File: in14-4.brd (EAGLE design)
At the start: 160 x 39 mm, 15 parts, among them IC1 4094D, IC2 4094D, Q1 K155ID1, Q2 K155ID1, Q3 K155ID1, Q4 K155ID1

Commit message: Existing files added
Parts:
- moved IC2 24.5 mm to (97.3, 30.2)
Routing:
- net N$34: track 0.00 -> 50.4 mm
- net N$33: track 0.00 -> 44.9 mm
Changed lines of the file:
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@@
 <setting verticaltext="up"/>
 </settings>
-<grid distance="0.00625" unitdist="inch" unit="inch" style="dots" multiple="1" display="yes" altdistance="0.025" altunitdist="inch" altunit="inch"/>
+<grid distance="0.0125" unitdist="inch" unit="inch" style="dots" multiple="1" display="yes" altdistance="0.025" altunitdist="inch" altunit="inch"/>
 <layers>
 <layer number="1" name="Top" color="4" fill="1" visible="yes" active="yes"/>
@@
 <element name="Q4" library="nixie" package="DIL16" value="K155ID1" x="110.49" y="54.61" rot="MR180"/>
 <element name="UL4" library="nixie" package="IN-14" value="IN-14" x="110.49" y="40.64" rot="R180"/>
-<element name="IC2" library="40xx" package="SO16" value="4094D" x="72.86625" y="30.7975" rot="MR180"/>
+<element name="IC2" library="40xx" package="SO16" value="4094D" x="97.31375" y="30.1625" rot="MR180"/>
 <element name="R3" library="rcl" package="R1206" value="10K" x="82.55" y="33.02" rot="MR0"/>
 <element name="R4" library="rcl" package="R1206" value="10K" x="106.68" y="33.02" rot="MR0"/>
@@
 <wire x1="46.99" y1="59.69" x2="46.99" y2="58.42" width="0.4064" layer="1"/>
 <wire x1="87.63" y1="58.42" x2="111.76" y2="58.42" width="0" layer="19" extent="1-1"/>
-<wire x1="77.31125" y1="33.8709" x2="87.63" y2="58.42" width="0" layer="19" extent="16-16"/>
-<wire x1="68.42125" y1="27.7241" x2="77.31125" y2="33.8709" width="0" layer="19" extent="16-16"/>
-<wire x1="36.03625" y1="32.6009" x2="68.42125" y2="27.7241" width="0" layer="19" extent="16-16"/>
+<wire x1="101.75875" y1="33.2359" x2="87.63" y2="58.42" width="0" layer="19" extent="16-16"/>
+<wire x1="92.86875" y1="27.0891" x2="101.75875" y2="33.2359" width="0" layer="19" extent="16-16"/>
+<wire x1="36.03625" y1="32.6009" x2="92.86875" y2="27.0891" width="0" layer="19" extent="16-16"/>
 <wire x1="27.14625" y1="26.4541" x2="36.03625" y2="32.6009" width="0" layer="19" extent="16-16"/>
 <wire x1="7.62" y1="40.64" x2="27.14625" y2="26.4541" width="0" layer="19" extent="16-16"/>
@@
 <wire x1="11.43" y1="43.815" x2="9.525" y2="45.72" width="0.4064" layer="16"/>
 <wire x1="9.525" y1="45.72" x2="7.62" y2="45.72" width="0.4064" layer="16"/>
-<wire x1="29.68625" y1="33.81375" x2="70.96125" y2="33.8709" width="0" layer="19" extent="16-16"/>
+<wire x1="29.68625" y1="33.81375" x2="95.40875" y2="33.2359" width="0" layer="19" extent="16-16"/>
 </signal>
 <signal name="N$33">
@@
 <contactref element="JP1" pad="6"/>
 <contactref element="IC2" pad="1"/>
-<wire x1="27.14625" y1="32.6009" x2="68.42125" y2="33.8709" width="0" layer="19" extent="16-16"/>
-<wire x1="7.62" y1="48.26" x2="27.14625" y2="32.6009" width="0" layer="19" extent="16-16"/>
+<wire x1="27.14625" y1="32.6009" x2="26.09215" y2="32.6009" width="0.4064" layer="16"/>
+<wire x1="26.09215" y1="32.6009" x2="22.38375" y2="28.8925" width="0.4064" layer="16"/>
+<wire x1="22.38375" y1="28.8925" x2="21.11375" y2="28.8925" width="0.4064" layer="16"/>
+<wire x1="21.11375" y1="28.8925" x2="19.05" y2="26.82875" width="0.4064" layer="16"/>
+<wire x1="19.05" y1="26.82875" x2="10.95375" y2="26.82875" width="0.4064" layer="16"/>
+<wire x1="10.95375" y1="26.82875" x2="4.7625" y2="33.02" width="0.4064" layer="16"/>
+<wire x1="4.7625" y1="33.02" x2="4.7625" y2="47.3075" width="0.4064" layer="16"/>
+<wire x1="4.7625" y1="47.3075" x2="5.715" y2="48.26" width="0.4064" layer="16"/>
+<wire x1="5.715" y1="48.26" x2="7.62" y2="48.26" width="0.4064" layer="16"/>
+<wire x1="27.14625" y1="32.6009" x2="92.86875" y2="33.2359" width="0" layer="19" extent="16-16"/>
 </signal>
 <signal name="N$34">
@@
 <contactref element="IC1" pad="15"/>
 <contactref element="IC2" pad="15"/>
-<wire x1="28.41625" y1="26.4541" x2="69.69125" y2="27.7241" width="0" layer="19" extent="16-16"/>
-<wire x1="7.62" y1="50.8" x2="28.41625" y2="26.4541" width="0" layer="19" extent="16-16"/>
+<wire x1="28.41625" y1="26.4541" x2="28.41625" y2="27.46375" width="0.4064" layer="16"/>
+<wire x1="28.41625" y1="27.46375" x2="27.6225" y2="28.2575" width="0.4064" layer="16"/>
+<wire x1="27.6225" y1="28.2575" x2="23.1775" y2="28.2575" width="0.4064" layer="16"/>
+<wire x1="23.1775" y1="28.2575" x2="22.86" y2="27.94" width="0.4064" layer="16"/>
+<wire x1="22.86" y1="27.94" x2="21.2725" y2="27.94" width="0.4064" layer="16"/>
+<wire x1="21.2725" y1="27.94" x2="19.3675" y2="26.035" width="0.4064" layer="16"/>
+<wire x1="19.3675" y1="26.035" x2="10.4775" y2="26.035" width="0.4064" layer="16"/>
+<wire x1="10.4775" y1="26.035" x2="3.81" y2="32.7025" width="0.4064" layer="16"/>
+<wire x1="3.81" y1="32.7025" x2="3.81" y2="48.895" width="0.4064" layer="16"/>
+<wire x1="3.81" y1="48.895" x2="5.715" y2="50.8" width="0.4064" layer="16"/>
+<wire x1="5.715" y1="50.8" x2="7.62" y2="50.8" width="0.4064" layer="16"/>
+<wire x1="28.41625" y1="27.46375" x2="94.13875" y2="27.0891" width="0" layer="19" extent="16-16"/>
 </signal>
 <signal name="N$35">
 <contactref element="IC2" pad="7"/>
 <contactref element="Q3" pad="4"/>
-<wire x1="76.04125" y1="33.8709" x2="85.09" y2="58.42" width="0" layer="19" extent="16-16"/>
+<wire x1="100.48875" y1="33.2359" x2="85.09" y2="58.42" width="0" layer="19" extent="16-16"/>
 </signal>
 <signal name="N$37">
 <contactref element="IC2" pad="5"/>
 <contactref element="Q3" pad="6"/>
-<wire x1="73.50125" y1="33.8709" x2="90.17" y2="58.42" width="0" layer="19" extent="16-16"/>
+<wire x1="97.94875" y1="33.2359" x2="90.17" y2="58.42" width="0" layer="19" extent="16-16"/>
 </signal>
 <signal name="N$38">
 <contactref element="IC2" pad="4"/>
 <contactref element="Q3" pad="3"/>
-<wire x1="72.23125" y1="33.8709" x2="82.55" y2="58.42" width="0" layer="19" extent="16-16"/>
+<wire x1="96.67875" y1="33.2359" x2="82.55" y2="58.42" width="0" layer="19" extent="16-16"/>
 </signal>
 <signal name="N$39">
 <contactref element="IC2" pad="14"/>
 <contactref element="Q4" pad="3"/>
-<wire x1="70.96125" y1="27.7241" x2="106.68" y2="58.42" width="0" layer="19" extent="16-16"/>
+<wire x1="95.40875" y1="27.0891" x2="106.68" y2="58.42" width="0" layer="19" extent="16-16"/>
 </signal>
 <signal name="N$40">
 <contactref element="IC2" pad="13"/>
 <contactref element="Q4" pad="6"/>
-<wire x1="72.23125" y1="27.7241" x2="114.3" y2="58.42" width="0" layer="19" extent="16-16"/>
+<wire x1="96.67875" y1="27.0891" x2="114.3" y2="58.42" width="0" layer="19" extent="16-16"/>
 </signal>
 <signal name="N$41">
 <contactref element="IC2" pad="12"/>
 <contactref element="Q4" pad="7"/>
-<wire x1="73.50125" y1="27.7241" x2="116.84" y2="58.42" width="0" layer="19" extent="16-16"/>
+<wire x1="97.94875" y1="27.0891" x2="116.84" y2="58.42" width="0" layer="19" extent="16-16"/>
 </signal>
 <signal name="N$42">
 <contactref element="IC2" pad="11"/>
 <contactref element="Q4" pad="4"/>
-<wire x1="74.77125" y1="27.7241" x2="109.22" y2="58.42" width="0" layer="19" extent="16-16"/>
+<wire x1="99.21875" y1="27.0891" x2="109.22" y2="58.42" width="0" layer="19" extent="16-16"/>
 </signal>
 <signal name="N$43">
@@
 <contactref element="IC2" pad="2"/>
 <contactref element="IC1" pad="9"/>
-<wire x1="36.03625" y1="26.4541" x2="69.69125" y2="33.8709" width="0" layer="19" extent="16-16"/>
+<wire x1="36.03625" y1="26.4541" x2="94.13875" y2="33.2359" width="0" layer="19" extent="16-16"/>
 </signal>
 <signal name="N$36">
 <contactref element="IC2" pad="6"/>
 <contactref element="Q3" pad="7"/>
-<wire x1="74.77125" y1="33.8709" x2="92.71" y2="58.42" width="0" layer="19" extent="16-16"/>
+<wire x1="99.21875" y1="33.2359" x2="92.71" y2="58.42" width="0" layer="19" extent="16-16"/>
 </signal>
 <signal name="N$63">

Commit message: .
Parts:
- removed IC2: 4094D, 40xx:SO16
- added IC3: 4094D, 40xx:SO16
- moved IC1 65.1 mm to (96.7, 29.5)
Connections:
- removed net GND: JP1.8, Q1.12, Q2.12, Q3.12, Q4.12
- new net VDD: IC1.16, IC3.16
- new net VSS: IC1.8, IC3.8, JP1.8, Q1.12, Q2.12, Q3.12, Q4.12
- net +5V: no longer IC1.16, IC1.8, IC2.16, IC2.8
- net N$24: now also IC3.5; no longer IC1.5
- net N$28: now also IC3.13; no longer IC1.13
- net N$29: now also IC3.12; no longer IC1.12
- net N$30: now also IC3.11; no longer IC1.11
- net N$31: now also IC3.2; no longer IC1.2
- net N$32: now also IC3.3; no longer IC2.3
- net N$33: now also IC3.1; no longer IC2.1
- net N$34: now also IC3.15; no longer IC2.15
- net N$35: now also IC1.7; no longer IC2.7
- net N$36: now also IC1.6; no longer IC2.6
- net N$37: now also IC1.5; no longer IC2.5
- net N$38: now also IC1.4; no longer IC2.4
- net N$39: now also IC1.14; no longer IC2.14
- net N$40: now also IC1.13; no longer IC2.13
- net N$41: now also IC1.12; no longer IC2.12
- net N$42: now also IC1.11; no longer IC2.11
- net N$63: now also IC3.4; no longer IC1.4
- net N$67: now also IC1.2, IC3.9; no longer IC1.9, IC2.2
- net N$68: now also IC3.7; no longer IC1.7
- net N$69: now also IC3.6; no longer IC1.6
- net N$70: now also IC3.14; no longer IC1.14
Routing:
- net 200V: track 43.5 -> 114.8 mm, vias 2 -> 4
- net N$42: track 0.00 -> 70.6 mm
- net N$39: track 0.00 -> 68.1 mm
- net N$40: track 0.00 -> 60.4 mm
- net N$41: track 0.00 -> 58.5 mm
- net N$38: track 0.00 -> 33.8 mm
- net N$54: track 0.00 -> 33.0 mm
- net N$44: track 0.00 -> 33.0 mm
- net N$36: track 0.00 -> 29.7 mm
- net N$37: track 0.00 -> 27.1 mm
- net N$23: track 0.00 -> 21.0 mm, vias 0 -> 1
- net N$62: track 0.00 -> 21.0 mm, vias 0 -> 1
- net N$55: track 0.00 -> 20.0 mm
- net N$45: track 0.00 -> 20.0 mm
- net N$35: track 0.00 -> 17.7 mm
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
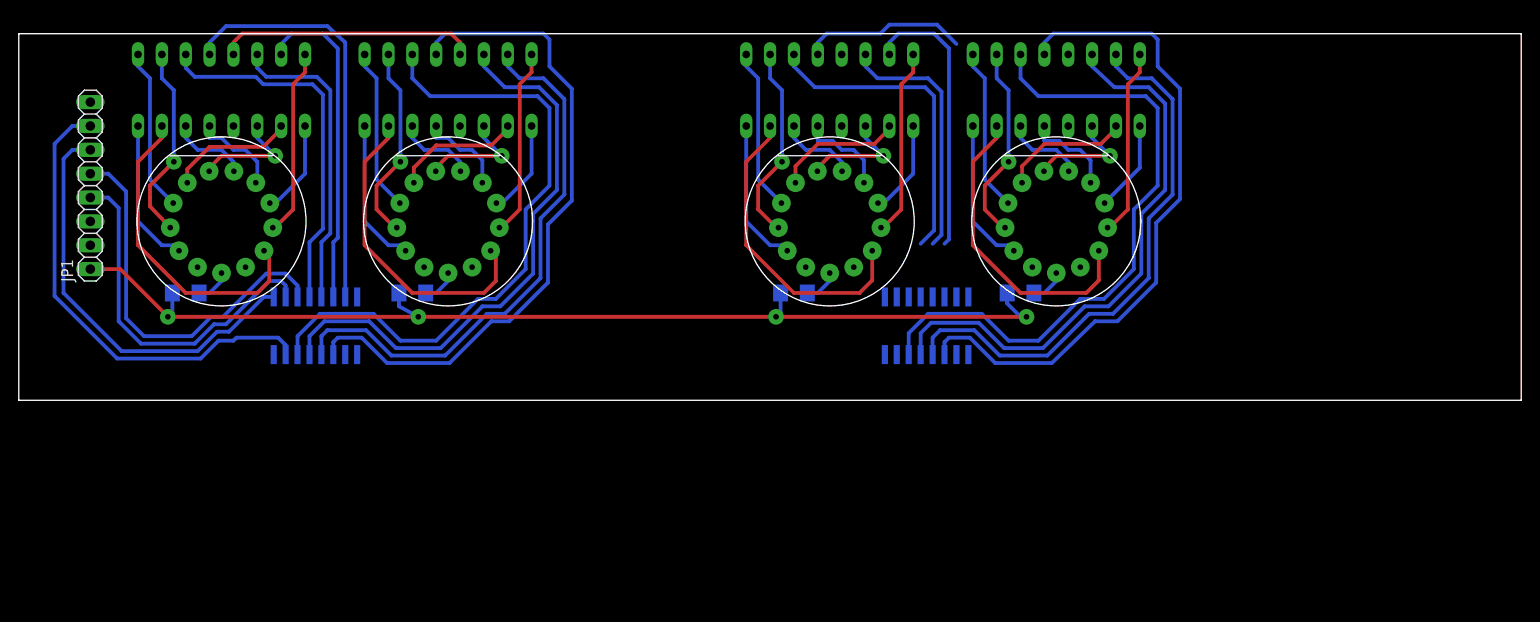
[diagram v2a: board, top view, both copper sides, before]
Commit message: Fixing ERC errors
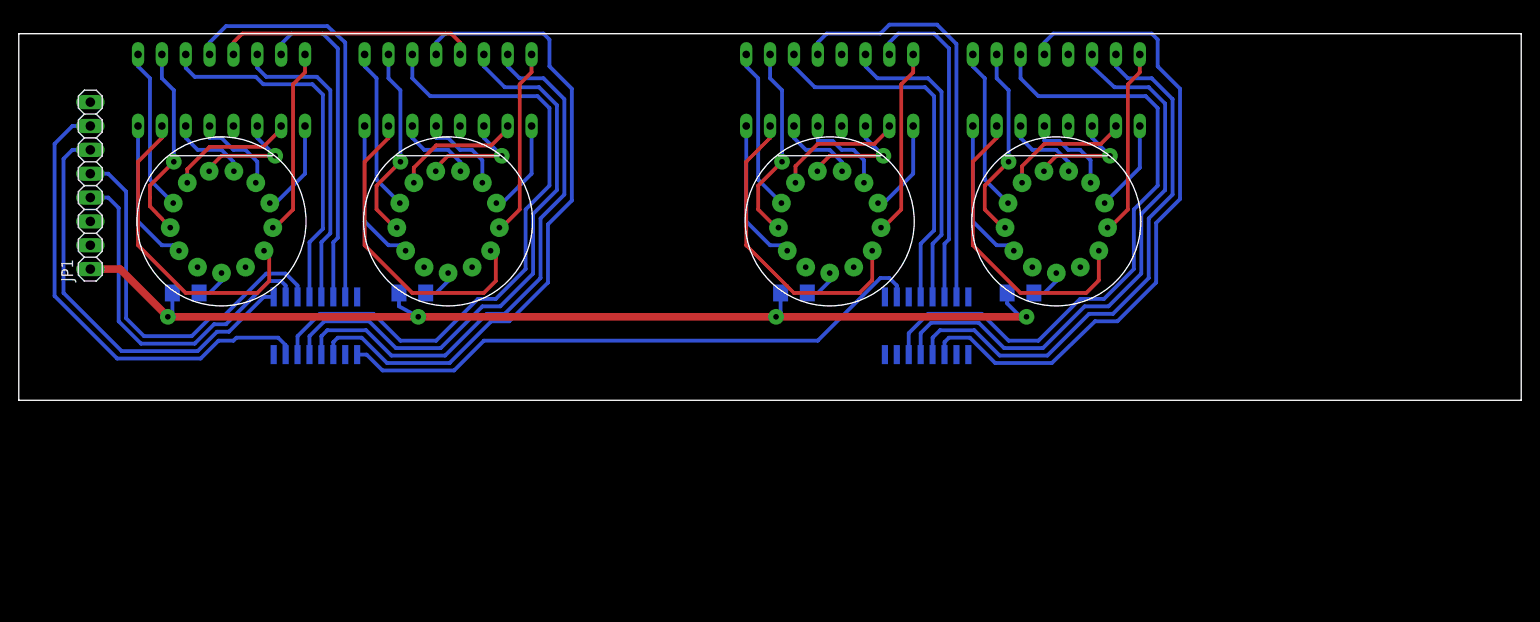
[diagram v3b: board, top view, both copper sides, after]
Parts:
- JP1: value (none) -> CON
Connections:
- net VSS renamed GND
- removed net VDD: IC1.16, IC3.16
- net +5V: now also IC1.16, IC3.16
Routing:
- net N$67: track 0.00 -> 63.8 mm
- net N$35: track 17.7 -> 44.6 mm
- net N$36: track 29.7 -> 35.3 mm
- net N$38: track 33.8 -> 39.5 mm
- net N$37: track 27.1 -> 32.7 mm
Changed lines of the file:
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@@
 <element name="UL2" library="nixie" package="IN-14" value="IN-14" x="45.72" y="40.64" rot="R180"/>
 <element name="Q2" library="nixie" package="DIL16" value="K155ID1" x="45.72" y="54.61" rot="MR180"/>
-<element name="JP1" library="pinhead" package="1X08" value="" x="7.62" y="44.45" rot="R90"/>
+<element name="JP1" library="pinhead" package="1X08" value="CON" x="7.62" y="44.45" rot="R90"/>
 <element name="Q3" library="nixie" package="DIL16" value="K155ID1" x="86.36" y="54.61" rot="MR180"/>
 <element name="UL3" library="nixie" package="IN-14" value="IN-14" x="86.36" y="40.64" rot="R180"/>
@@
 <wire x1="46.0375" y1="60.6425" x2="46.99" y2="59.69" width="0.4064" layer="1"/>
 <wire x1="46.99" y1="59.69" x2="46.99" y2="58.42" width="0.4064" layer="1"/>
+<contactref element="IC3" pad="16"/>
+<contactref element="IC1" pad="16"/>
 <wire x1="87.63" y1="58.42" x2="111.76" y2="58.42" width="0" layer="19" extent="1-1"/>
+<wire x1="92.23375" y1="26.4541" x2="87.63" y2="58.42" width="0" layer="19" extent="16-16"/>
 <wire x1="46.99" y1="58.42" x2="87.63" y2="58.42" width="0" layer="19" extent="1-1"/>
 <wire x1="7.62" y1="40.64" x2="22.86" y2="58.42" width="0" layer="19" extent="1-1"/>
+<wire x1="27.14625" y1="26.4541" x2="7.62" y2="40.64" width="0" layer="19" extent="16-16"/>
 </signal>
 <signal name="N$1">
@@
 <wire x1="16.358" y1="33.02" x2="16.358" y2="30.963" width="0.4064" layer="16"/>
 <wire x1="16.358" y1="30.963" x2="15.875" y2="30.48" width="0.4064" layer="16"/>
-<wire x1="7.62" y1="35.56" x2="10.795" y2="35.56" width="0.4064" layer="1"/>
-<wire x1="10.795" y1="35.56" x2="15.875" y2="30.48" width="0.4064" layer="1"/>
+<wire x1="7.62" y1="35.56" x2="10.795" y2="35.56" width="0.8128" layer="1"/>
+<wire x1="10.795" y1="35.56" x2="15.875" y2="30.48" width="0.8128" layer="1"/>
 <via x="42.545" y="30.48" extent="1-16" drill="0.6" diameter="1.6764"/>
 <wire x1="40.488" y1="33.02" x2="40.488" y2="31.598" width="0.4064" layer="16"/>
 <wire x1="40.488" y1="31.598" x2="42.545" y2="30.48" width="0.4064" layer="16"/>
-<wire x1="15.875" y1="30.48" x2="42.545" y2="30.48" width="0.4064" layer="1"/>
+<wire x1="15.875" y1="30.48" x2="42.545" y2="30.48" width="0.8128" layer="1"/>
 <via x="80.645" y="30.48" extent="1-16" drill="0.6" diameter="1.6764"/>
 <wire x1="81.128" y1="33.02" x2="81.128" y2="30.963" width="0.4064" layer="16"/>
@@
 <via x="107.315" y="30.48" extent="1-16" drill="0.6" diameter="1.6764"/>
 <wire x1="106.68" y1="30.48" x2="107.315" y2="30.48" width="0.4064" layer="16"/>
-<wire x1="42.545" y1="30.48" x2="80.645" y2="30.48" width="0.4064" layer="1"/>
-<wire x1="80.645" y1="30.48" x2="107.315" y2="30.48" width="0.4064" layer="1"/>
+<wire x1="42.545" y1="30.48" x2="80.645" y2="30.48" width="0.8128" layer="1"/>
+<wire x1="80.645" y1="30.48" x2="107.315" y2="30.48" width="0.8128" layer="1"/>
 </signal>
 <signal name="N$12">
@@
 <wire x1="5.715" y1="50.8" x2="7.62" y2="50.8" width="0.4064" layer="16"/>
 <contactref element="IC3" pad="15"/>
+<wire x1="28.41625" y1="26.4541" x2="28.41625" y2="27.46375" width="0.4064" layer="16"/>
 <contactref element="IC1" pad="15"/>
-<wire x1="28.41625" y1="26.4541" x2="28.41625" y2="27.46375" width="0.4064" layer="16"/>
 <wire x1="28.41625" y1="26.4541" x2="93.50375" y2="26.4541" width="0" layer="19" extent="16-16"/>
 </signal>
@@
 <wire x1="85.09" y1="59.69" x2="85.09" y2="58.42" width="0.4064" layer="16"/>
 <contactref element="IC1" pad="7"/>
-<wire x1="99.85375" y1="32.6009" x2="99.85375" y2="59.53125" width="0" layer="19" extent="16-16"/>
+<wire x1="99.85375" y1="32.6009" x2="99.85375" y2="59.53125" width="0.4064" layer="16"/>
 </signal>
 <signal name="N$37">
@@
 <wire x1="90.17" y1="57.15" x2="90.17" y2="58.42" width="0.4064" layer="16"/>
 <contactref element="IC1" pad="5"/>
-<wire x1="97.31375" y1="32.6009" x2="97.31375" y2="38.25875" width="0" layer="19" extent="16-16"/>
+<wire x1="97.31375" y1="32.6009" x2="97.31375" y2="38.25875" width="0.4064" layer="16"/>
 </signal>
 <signal name="N$38">
@@
 <wire x1="82.55" y1="57.15" x2="82.55" y2="58.42" width="0.4064" layer="16"/>
 <contactref element="IC1" pad="4"/>
-<wire x1="96.04375" y1="32.6009" x2="96.04375" y2="38.25875" width="0" layer="19" extent="16-16"/>
+<wire x1="96.04375" y1="32.6009" x2="96.04375" y2="38.25875" width="0.4064" layer="16"/>
 </signal>
 <signal name="N$39">
@@
 <contactref element="IC3" pad="9"/>
 <contactref element="IC1" pad="2"/>
-<wire x1="36.03625" y1="26.4541" x2="93.50375" y2="32.6009" width="0" layer="19" extent="16-16"/>
+<wire x1="36.03625" y1="26.4541" x2="37.0459" y2="26.4541" width="0.4064" layer="16"/>
+<wire x1="37.0459" y1="26.4541" x2="38.735" y2="24.765" width="0.4064" layer="16"/>
+<wire x1="38.735" y1="24.765" x2="46.355" y2="24.765" width="0.4064" layer="16"/>
+<wire x1="46.355" y1="24.765" x2="49.53" y2="27.94" width="0.4064" layer="16"/>
+<wire x1="49.53" y1="27.94" x2="85.09" y2="27.94" width="0.4064" layer="16"/>
+<wire x1="85.09" y1="27.94" x2="91.7575" y2="34.6075" width="0.4064" layer="16"/>
+<wire x1="93.50375" y1="32.6009" x2="93.50375" y2="33.81375" width="0.4064" layer="16"/>
+<wire x1="93.50375" y1="33.81375" x2="92.71" y2="34.6075" width="0.4064" layer="16"/>
+<wire x1="92.71" y1="34.6075" x2="91.7575" y2="34.6075" width="0.4064" layer="16"/>
 </signal>
 <signal name="N$36">
@@
 <wire x1="92.71" y1="59.69" x2="92.71" y2="58.42" width="0.4064" layer="16"/>
 <contactref element="IC1" pad="6"/>
-<wire x1="98.58375" y1="32.6009" x2="98.58375" y2="38.25875" width="0" layer="19" extent="16-16"/>
+<wire x1="98.58375" y1="32.6009" x2="98.58375" y2="38.25875" width="0.4064" layer="16"/>
 </signal>
 <signal name="N$63">
@@
 <wire x1="86.36" y1="47.625" x2="92.075" y2="47.625" width="0.4064" layer="1"/>
 </signal>
-<signal name="VSS">
+<signal name="GND">
+<contactref element="Q2" pad="12"/>
+<contactref element="Q3" pad="12"/>
+<contactref element="Q1" pad="12"/>
+<contactref element="JP1" pad="8"/>
 <contactref element="IC3" pad="8"/>
+<contactref element="Q4" pad="12"/>
 <contactref element="IC1" pad="8"/>
-<contactref element="Q1" pad="12"/>
-<contactref element="Q2" pad="12"/>
-<contactref element="JP1" pad="8"/>
-<contactref element="Q3" pad="12"/>
-<contactref element="Q4" pad="12"/>
 <wire x1="101.12375" y1="32.6009" x2="111.76" y2="50.8" width="0" layer="19" extent="16-16"/>
 <wire x1="87.63" y1="50.8" x2="101.12375" y2="32.6009" width="0" layer="19" extent="16-16"/>
@@
 <wire x1="7.62" y1="53.34" x2="22.86" y2="50.8" width="0" layer="19" extent="1-1"/>
 </signal>
-<signal name="VDD">
-<contactref element="IC3" pad="16"/>
-<contactref element="IC1" pad="16"/>
-<wire x1="27.14625" y1="26.4541" x2="92.23375" y2="26.4541" width="0" layer="19" extent="16-16"/>
-</signal>
 </signals>
